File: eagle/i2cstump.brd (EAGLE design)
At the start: 31.2 x 19 mm, 20 parts, among them IC1 ATTINY85, IC2 REG1117, Q1 220mA/50V/3.5Ω, Q2 220mA/50V/3.5Ω, X1 USBPCB

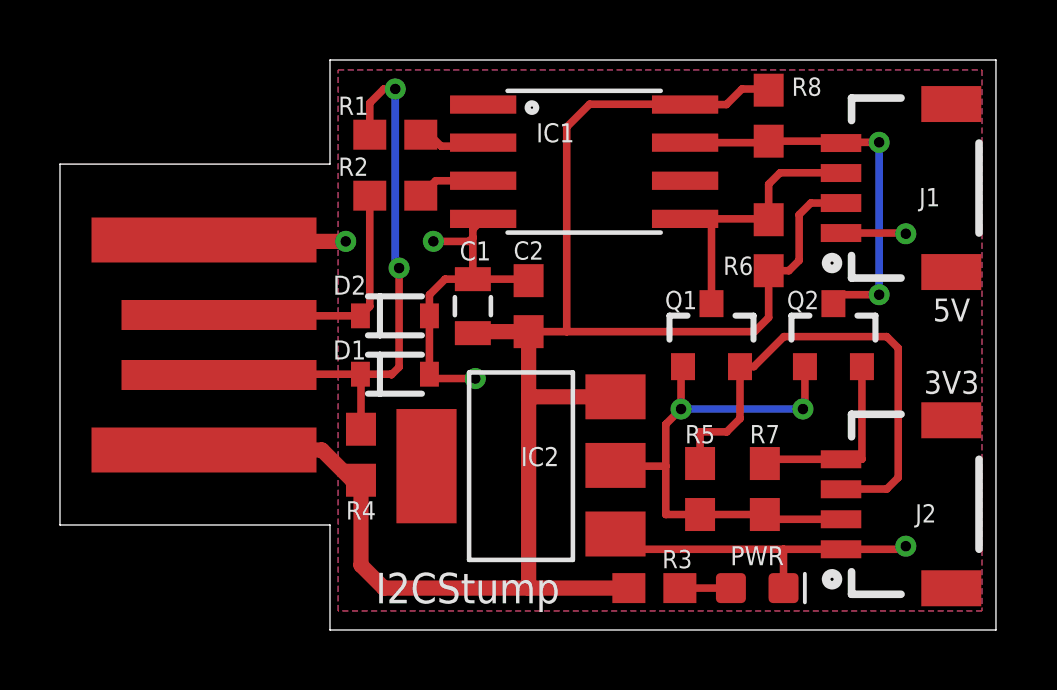
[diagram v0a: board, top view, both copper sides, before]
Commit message: Clean up schematic -- split out the levelshifter from the 5V pullups
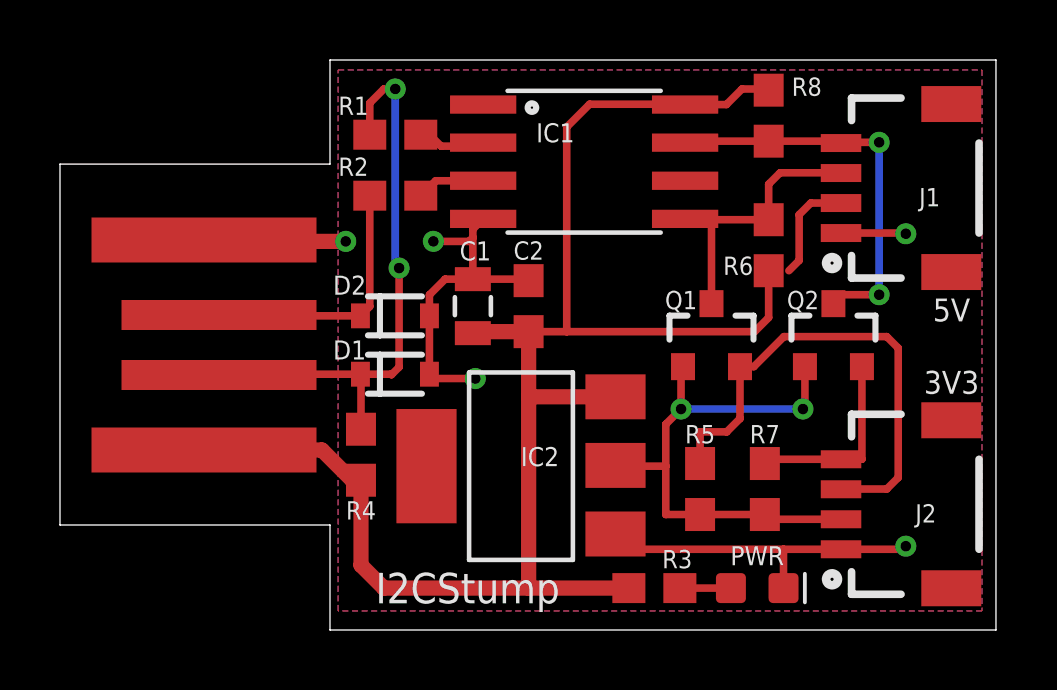
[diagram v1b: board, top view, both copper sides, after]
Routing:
- net 5V: track 59.6 -> 58.9 mm
- net +3V3: track 19.3 -> 18.6 mm
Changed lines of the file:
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@@
 <drawing>
 <settings>
-<setting alwaysvectorfont="yes"/>
+<setting alwaysvectorfont="no"/>
 <setting keepoldvectorfont="yes"/>
 <setting verticaltext="up"/>
@@
 <contactref element="J1" pad="2"/>
 <contactref element="IC2" pad="3"/>
-<contactref element="R6" pad="2"/>
-<contactref element="R8" pad="2"/>
 <wire x1="23.622" y1="18.377" x2="23.622" y2="18.034" width="0.254" layer="1"/>
 <contactref element="R4" pad="2"/>
 <contactref element="X1" pad="5V"/>
-<wire x1="23.622" y1="18.034" x2="23.622" y2="17.995" width="0.254" layer="1"/>
 <wire x1="4.8" y1="6.096" x2="4.8" y2="6" width="0.254" layer="1"/>
 <contactref element="C2" pad="1"/>
@@
 <wire x1="17.653" y1="17.526" x2="20.8254" y2="17.526" width="0.254" layer="1"/>
 <wire x1="20.8254" y1="17.526" x2="20.8368" y2="17.5146" width="0.254" layer="1"/>
-<wire x1="23.622" y1="11.977" x2="24.296" y2="11.977" width="0.254" layer="1"/>
 <wire x1="24.296" y1="11.977" x2="24.638" y2="12.319" width="0.254" layer="1"/>
 <wire x1="24.638" y1="12.319" x2="24.638" y2="13.843" width="0.254" layer="1"/>
@@
 <wire x1="15.621" y1="9.945" x2="16.891" y2="9.945" width="0.254" layer="1"/>
 <wire x1="16.891" y1="9.945" x2="23.153" y2="9.945" width="0.254" layer="1"/>
-<wire x1="23.153" y1="9.945" x2="23.622" y2="10.414" width="0.254" layer="1"/>
-<wire x1="23.622" y1="10.414" x2="23.622" y2="11.977" width="0.254" layer="1"/>
+<wire x1="23.622" y1="10.414" x2="23.153" y2="9.945" width="0.254" layer="1"/>
 <wire x1="16.891" y1="16.764" x2="16.891" y2="9.945" width="0.254" layer="1"/>
 <wire x1="10.033" y1="4.992" x2="10.033" y2="2.159" width="0.508" layer="1"/>
@@
 <vertex x="9.271" y="0.635"/>
 </polygon>
+<contactref element="R8" pad="2"/>
+<contactref element="R6" pad="2"/>
+<wire x1="23.622" y1="11.977" x2="23.622" y2="10.414" width="0.254" layer="1"/>
 </signal>
 <signal name="N$1">
@@
 <contactref element="J1" pad="3"/>
 <contactref element="IC1" pad="5"/>
+<wire x1="20.8368" y1="13.7046" x2="21.717" y2="13.7046" width="0.254" layer="1"/>
+<wire x1="24.003" y1="15.24" x2="23.622" y2="14.859" width="0.254" layer="1"/>
+<wire x1="24.003" y1="15.24" x2="26.027" y2="15.24" width="0.254" layer="1"/>
+<wire x1="26.027" y1="15.24" x2="26.035" y2="15.232" width="0.254" layer="1"/>
 <contactref element="Q1" pad="3"/>
 <contactref element="R6" pad="1"/>
-<wire x1="23.5944" y1="13.7046" x2="23.622" y2="13.677" width="0.254" layer="1"/>
-<wire x1="20.8368" y1="13.7046" x2="21.717" y2="13.7046" width="0.254" layer="1"/>
-<wire x1="21.717" y1="13.7046" x2="23.5944" y2="13.7046" width="0.254" layer="1"/>
-<wire x1="23.622" y1="13.677" x2="23.622" y2="14.859" width="0.254" layer="1"/>
-<wire x1="23.622" y1="14.859" x2="24.003" y2="15.24" width="0.254" layer="1"/>
-<wire x1="24.003" y1="15.24" x2="26.027" y2="15.24" width="0.254" layer="1"/>
-<wire x1="26.027" y1="15.24" x2="26.035" y2="15.232" width="0.254" layer="1"/>
 <wire x1="21.717" y1="10.879" x2="21.717" y2="13.7046" width="0.254" layer="1"/>
+<wire x1="23.622" y1="14.859" x2="23.622" y2="13.677" width="0.254" layer="1"/>
+<wire x1="23.622" y1="13.677" x2="21.7446" y2="13.677" width="0.254" layer="1"/>
+<wire x1="21.7446" y1="13.677" x2="21.717" y2="13.7046" width="0.254" layer="1"/>
 </signal>
 <signal name="N$6">
@@
 <contactref element="IC1" pad="7"/>
 <wire x1="26.035" y1="16.2446" x2="26.035" y2="16.232" width="0.254" layer="1"/>
-<contactref element="Q2" pad="3"/>
-<contactref element="R8" pad="1"/>
-<wire x1="20.8368" y1="16.2446" x2="23.622" y2="16.2446" width="0.254" layer="1"/>
-<wire x1="23.622" y1="16.2446" x2="23.622" y2="16.295" width="0.254" layer="1"/>
-<wire x1="23.622" y1="16.295" x2="25.972" y2="16.295" width="0.254" layer="1"/>
-<wire x1="25.972" y1="16.295" x2="26.035" y2="16.232" width="0.254" layer="1"/>
-<wire x1="25.824" y1="10.922" x2="25.781" y2="10.879" width="0.254" layer="1"/>
-<wire x1="25.781" y1="10.879" x2="26.078" y2="11.176" width="0.254" layer="1"/>
-<wire x1="26.078" y1="11.176" x2="27.305" y2="11.176" width="0.254" layer="1"/>
 <via x="27.305" y="11.176" extent="1-16" drill="0.35"/>
 <wire x1="27.305" y1="11.176" x2="27.305" y2="16.256" width="0.254" layer="16"/>
@@
 <wire x1="27.305" y1="16.256" x2="26.0464" y2="16.256" width="0.254" layer="1"/>
 <wire x1="26.0464" y1="16.256" x2="26.035" y2="16.2446" width="0.254" layer="1"/>
+<contactref element="Q2" pad="3"/>
+<contactref element="R8" pad="1"/>
+<wire x1="25.972" y1="16.295" x2="26.035" y2="16.232" width="0.254" layer="1"/>
+<wire x1="27.305" y1="11.176" x2="26.078" y2="11.176" width="0.254" layer="1"/>
+<wire x1="26.078" y1="11.176" x2="25.781" y2="10.879" width="0.254" layer="1"/>
+<wire x1="23.622" y1="16.295" x2="25.972" y2="16.295" width="0.254" layer="1"/>
+<wire x1="23.622" y1="16.295" x2="20.8872" y2="16.295" width="0.254" layer="1"/>
+<wire x1="20.8872" y1="16.295" x2="20.8368" y2="16.2446" width="0.254" layer="1"/>
 </signal>
 <signal name="+3V3">
@@
 <contactref element="Q1" pad="1"/>
 <contactref element="Q2" pad="1"/>
-<contactref element="R5" pad="2"/>
 <wire x1="20.767" y1="8.779" x2="20.828" y2="8.779" width="0.254" layer="1"/>
-<wire x1="18.5166" y1="6.096" x2="18.5166" y2="5.4864" width="0.254" layer="1"/>
-<contactref element="R7" pad="2"/>
-<wire x1="26.035" y1="3.691" x2="23.495" y2="3.691" width="0.254" layer="1"/>
-<wire x1="23.495" y1="3.691" x2="23.495" y2="3.849" width="0.254" layer="1"/>
-<wire x1="23.495" y1="3.849" x2="21.336" y2="3.849" width="0.254" layer="1"/>
-<wire x1="21.336" y1="3.849" x2="21.336" y2="3.937" width="0.254" layer="1"/>
-<wire x1="18.5166" y1="5.359403125" x2="18.5166" y2="5.4864" width="0.254" layer="1"/>
+<wire x1="23.749" y1="3.691" x2="23.495" y2="3.691" width="0.254" layer="1"/>
 <wire x1="20.767" y1="8.779" x2="20.701" y2="8.713" width="0.254" layer="1"/>
 <via x="20.701" y="7.366" extent="1-16" drill="0.35"/>
@@
 <wire x1="20.701" y1="8.713" x2="20.701" y2="7.366" width="0.254" layer="1"/>
 <wire x1="20.193" y1="6.858" x2="20.701" y2="7.366" width="0.254" layer="1"/>
-<wire x1="21.336" y1="3.849" x2="20.193" y2="3.849" width="0.254" layer="1"/>
-<wire x1="20.193" y1="3.849" x2="20.193" y2="5.461" width="0.254" layer="1"/>
-<wire x1="20.193" y1="5.461" x2="20.193" y2="6.858" width="0.254" layer="1"/>
-<wire x1="20.193" y1="5.461" x2="18.5166" y2="5.461" width="0.254" layer="1"/>
+<wire x1="20.193" y1="6.858" x2="20.193" y2="5.461" width="0.254" layer="1"/>
+<wire x1="20.193" y1="5.461" x2="20.193" y2="3.849" width="0.254" layer="1"/>
 <wire x1="18.5166" y1="5.461" x2="18.5166" y2="5.4864" width="0.254" layer="1"/>
+<contactref element="R5" pad="2"/>
+<contactref element="R7" pad="2"/>
+<wire x1="20.193" y1="3.849" x2="21.336" y2="3.849" width="0.254" layer="1"/>
+<wire x1="18.5166" y1="5.4864" x2="18.542" y2="5.461" width="0.254" layer="1"/>
+<wire x1="18.542" y1="5.461" x2="20.193" y2="5.461" width="0.254" layer="1"/>
+<wire x1="26.035" y1="3.691" x2="23.749" y2="3.691" width="0.254" layer="1"/>
+<wire x1="23.591" y1="3.849" x2="23.749" y2="3.691" width="0.254" layer="1"/>
+<wire x1="23.495" y1="3.849" x2="21.336" y2="3.849" width="0.254" layer="1"/>
+<wire x1="23.495" y1="3.849" x2="23.591" y2="3.849" width="0.254" layer="1"/>
 </signal>
 <signal name="SDA33">

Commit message: Cleanup BRD -- remove stubs, remove redundant 5V traces (they are on the top plane), widen 5V and GND traces to 0.02
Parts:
- moved C2 2.92 mm to (18.5, 10.8)
- moved C1 1.91 mm to (15.7, 10.7)
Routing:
- net 5V: track 58.9 -> 5.99 mm
- net GND: track 30.0 -> 31.4 mm, vias 5 -> 4
- net SDA33: track 16.5 -> 16.0 mm

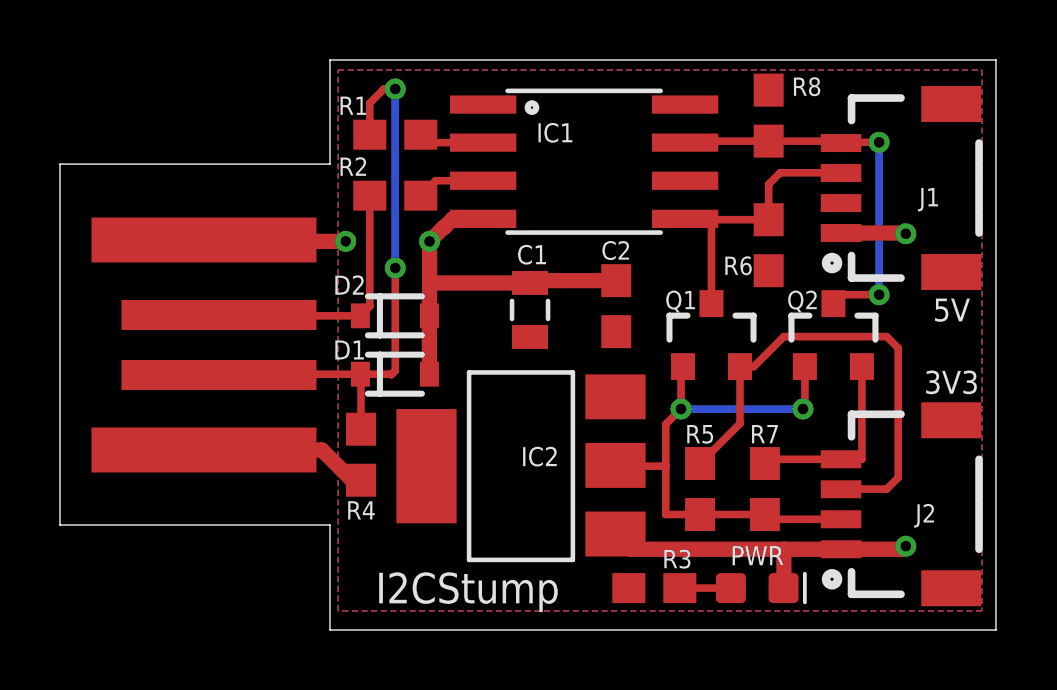
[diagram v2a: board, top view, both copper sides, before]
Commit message: Add some more GND via's - name USB_M and USB_P; Move AM1117 a bit so that 5V has more copper on ingress
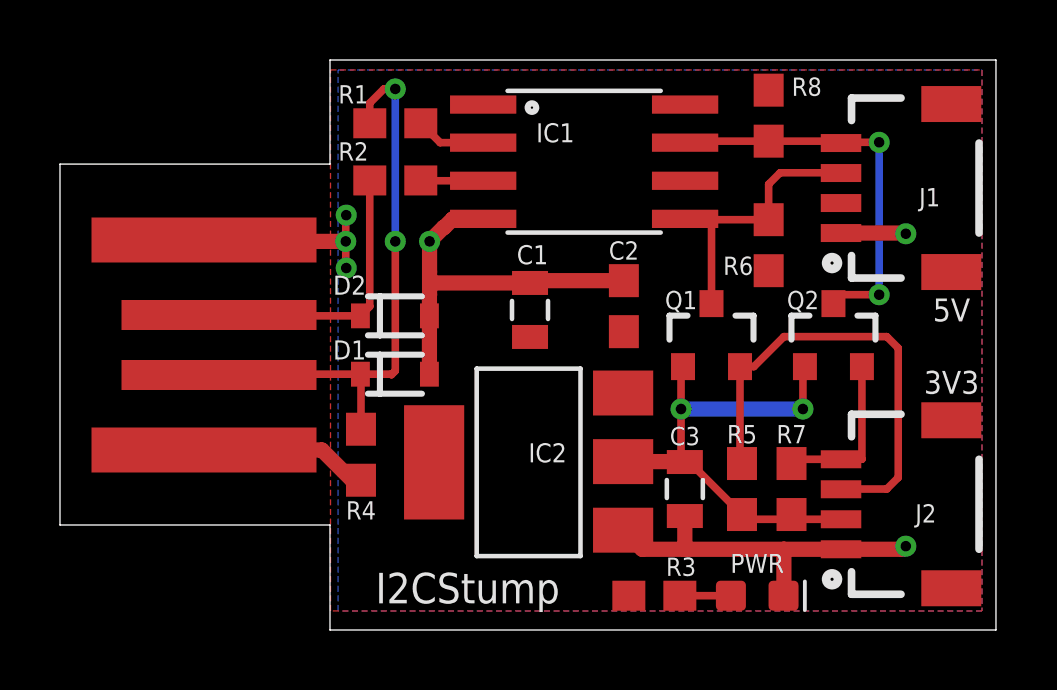
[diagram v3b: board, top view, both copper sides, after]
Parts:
- added C3: 4.7uf, SparkFun:0805
- J1: value (none) -> I2C-5V
- J2: value (none) -> I2C-3V3
- moved R5 1.40 mm to (22.7, 4.70)
- moved R7 0.89 mm to (24.4, 4.70)
- moved R2 0.51 mm to (11.2, 15.0)
- moved R1 0.38 mm to (11.2, 16.9)
- moved IC2 0.28 mm to (15.6, 5.59)
- moved D3 0.25 mm to (23.2, 1.14)
- moved R3 0.25 mm to (19.8, 1.14)
- moved C2 0.25 mm to (18.8, 10.8)
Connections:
- net N$10 renamed USB_M
- net N$11 renamed USB_P
- net +3V3: now also C3.1
- net GND: now also C3.2
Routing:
- net GND: track 31.4 -> 34.6 mm, vias 4 -> 6
- net +3V3: track 18.3 -> 17.0 mm
- net SCL33: track 6.38 -> 5.49 mm
- net SDA33: track 16.0 -> 15.5 mm
- net USB_P: track 8.86 -> 9.37 mm
